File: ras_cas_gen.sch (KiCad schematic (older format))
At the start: 16 parts, among them U10 74HCT02, U11 74LS27, U4 74LS257, U5 74LS257, U6 74LS257, U7 74LS02, U8 74LS138, U9 MOS_6529

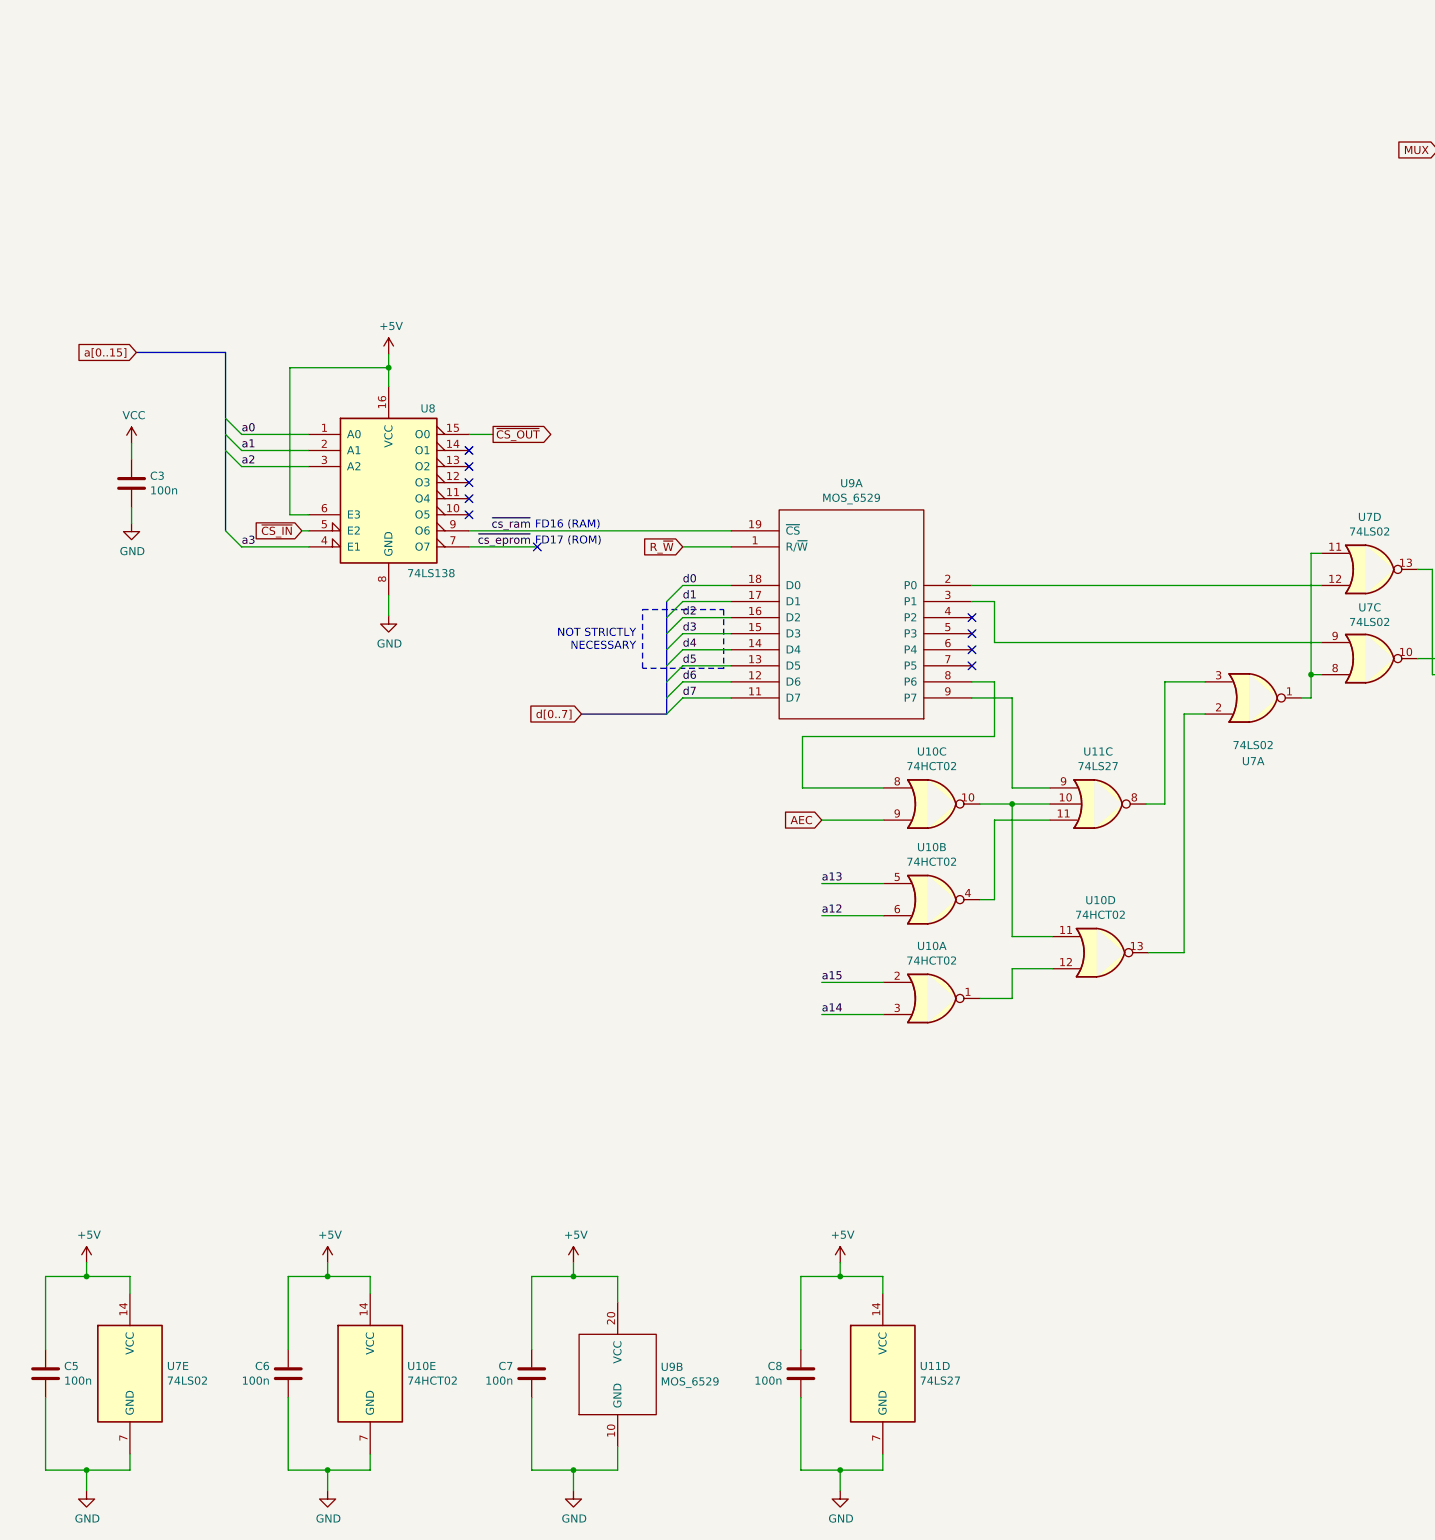
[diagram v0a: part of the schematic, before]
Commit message: Switch out the MOS 6529
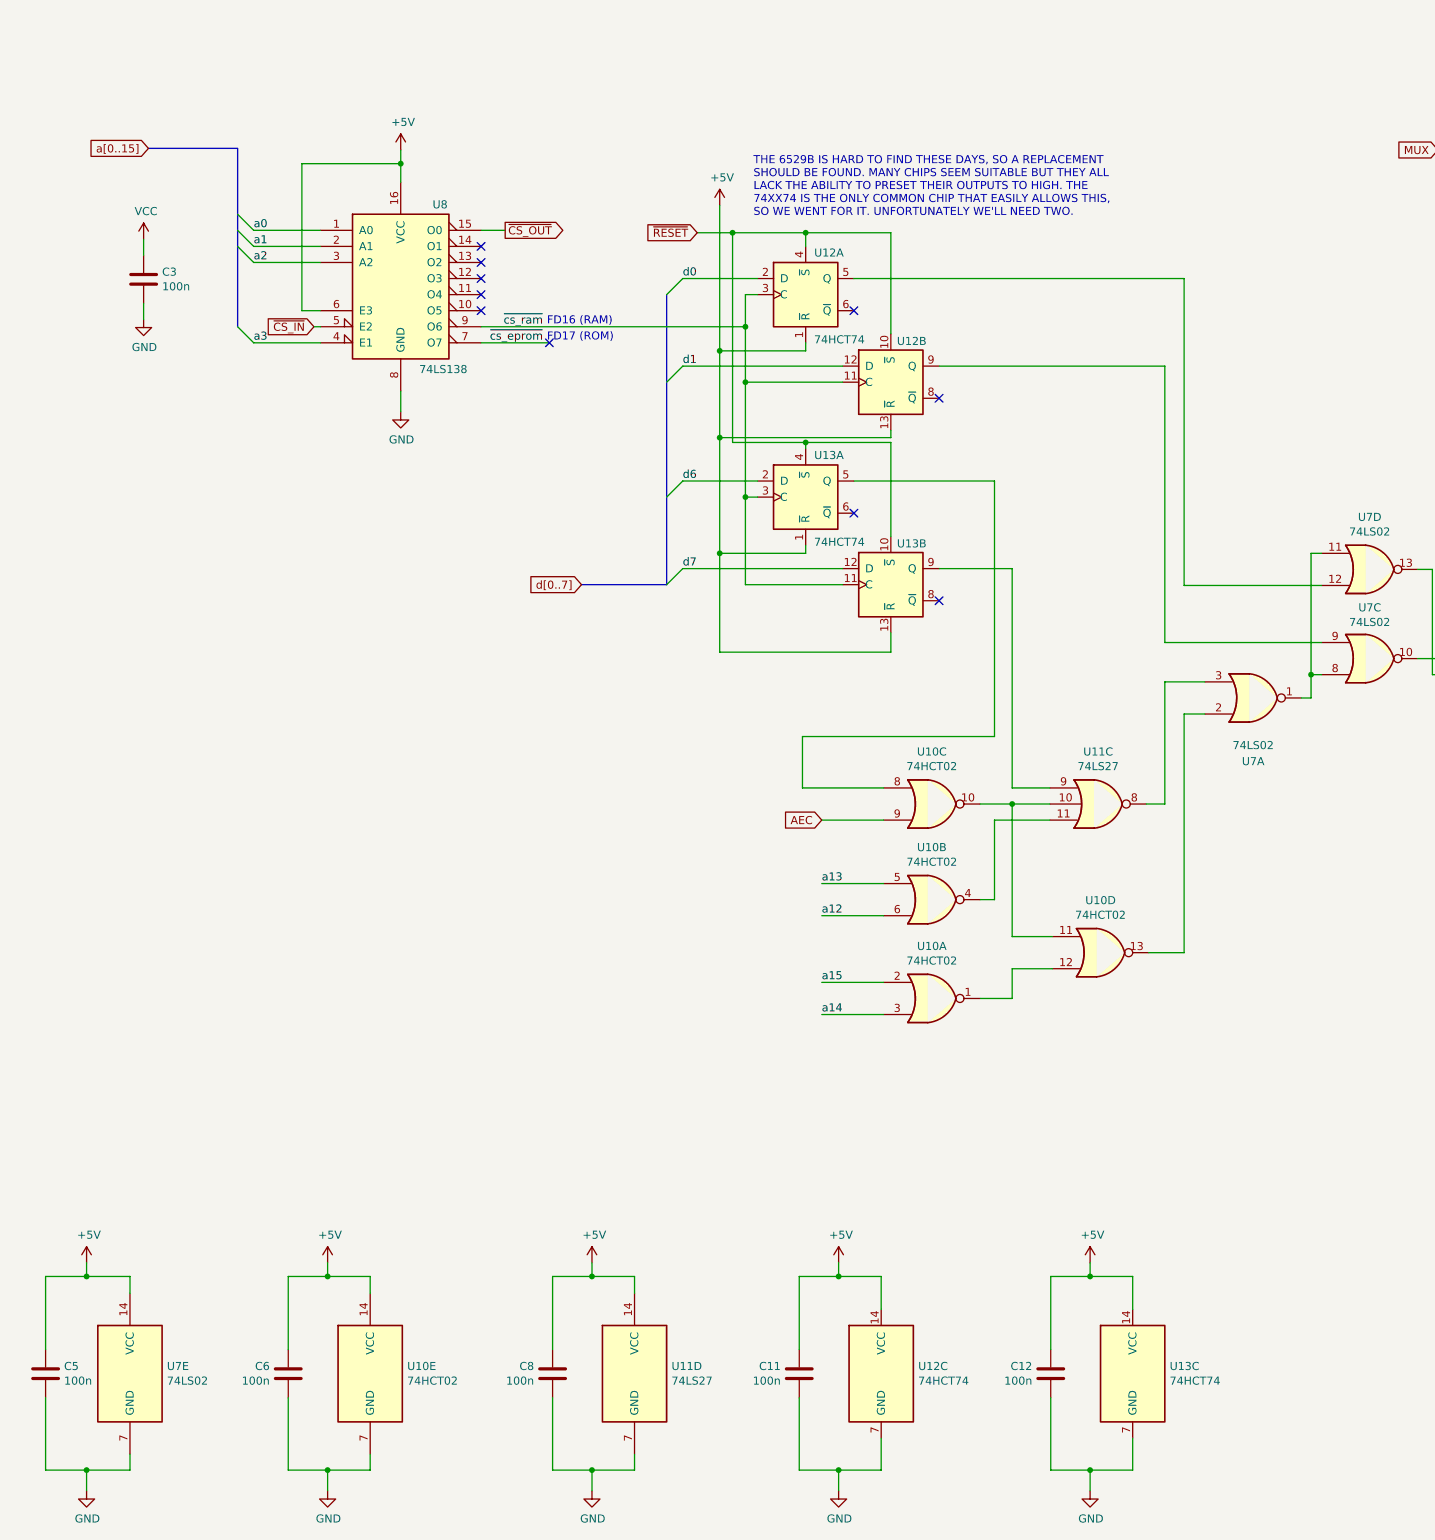
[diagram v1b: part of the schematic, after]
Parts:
- removed C7: 100n, symbol Device:C
- removed U9: MOS_6529, symbol MOS_6529:MOS_6529
- added C11, C12: 100n, symbol Device:C
- added U12, U13: 74HCT74, symbol 74xx:74LS74
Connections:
- net +5V: now also C11.1, C12.1, U12.1 (~R), U12.13 (~R), U12.14 (VCC), U13.1 (~R), U13.13 (~R), U13.14 (VCC)
- net GND: now also C11.2, C12.2, U12.7 (GND), U13.7 (GND)
- net d0: now also U12.2 (D)
- net d1: now also U12.12 (D)
- net d6: now also U13.2 (D)
- net d7: now also U13.12 (D)
- net ~cs_ram: now also U12.11 (C), U12.3 (C), U13.11 (C), U13.3 (C)
- net at U7.12: now also U12.5 (Q)
- net at U7.9: now also U12.9 (Q)
- net at U10.8: now also U13.5 (Q)
- net at U11.9: now also U13.9 (Q)
- new net ~RESET: U12.10 (~S), U12.4 (~S), U13.10 (~S), U13.4 (~S)
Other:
- note added: "THE 6529B IS HARD TO FIND THESE DAYS, SO A REPLACEMENT\nSHOULD BE FOUND. MANY CHIPS SEEM SUITABLE BUT THEY ALL\nLACK THE ABILITY TO PRESET THEIR OUTPUTS TO HIGH. THE\n74XX74 IS THE ONLY COMMON CHIP THAT EASILY ALLOWS THIS,\nSO WE WENT FOR IT. UNFORTUNATELY WE'LL NEED TWO."
- note removed: "NOT STRICTLY\nNECESSARY"
- moved on the sheet: C3, C8, U11D, U8

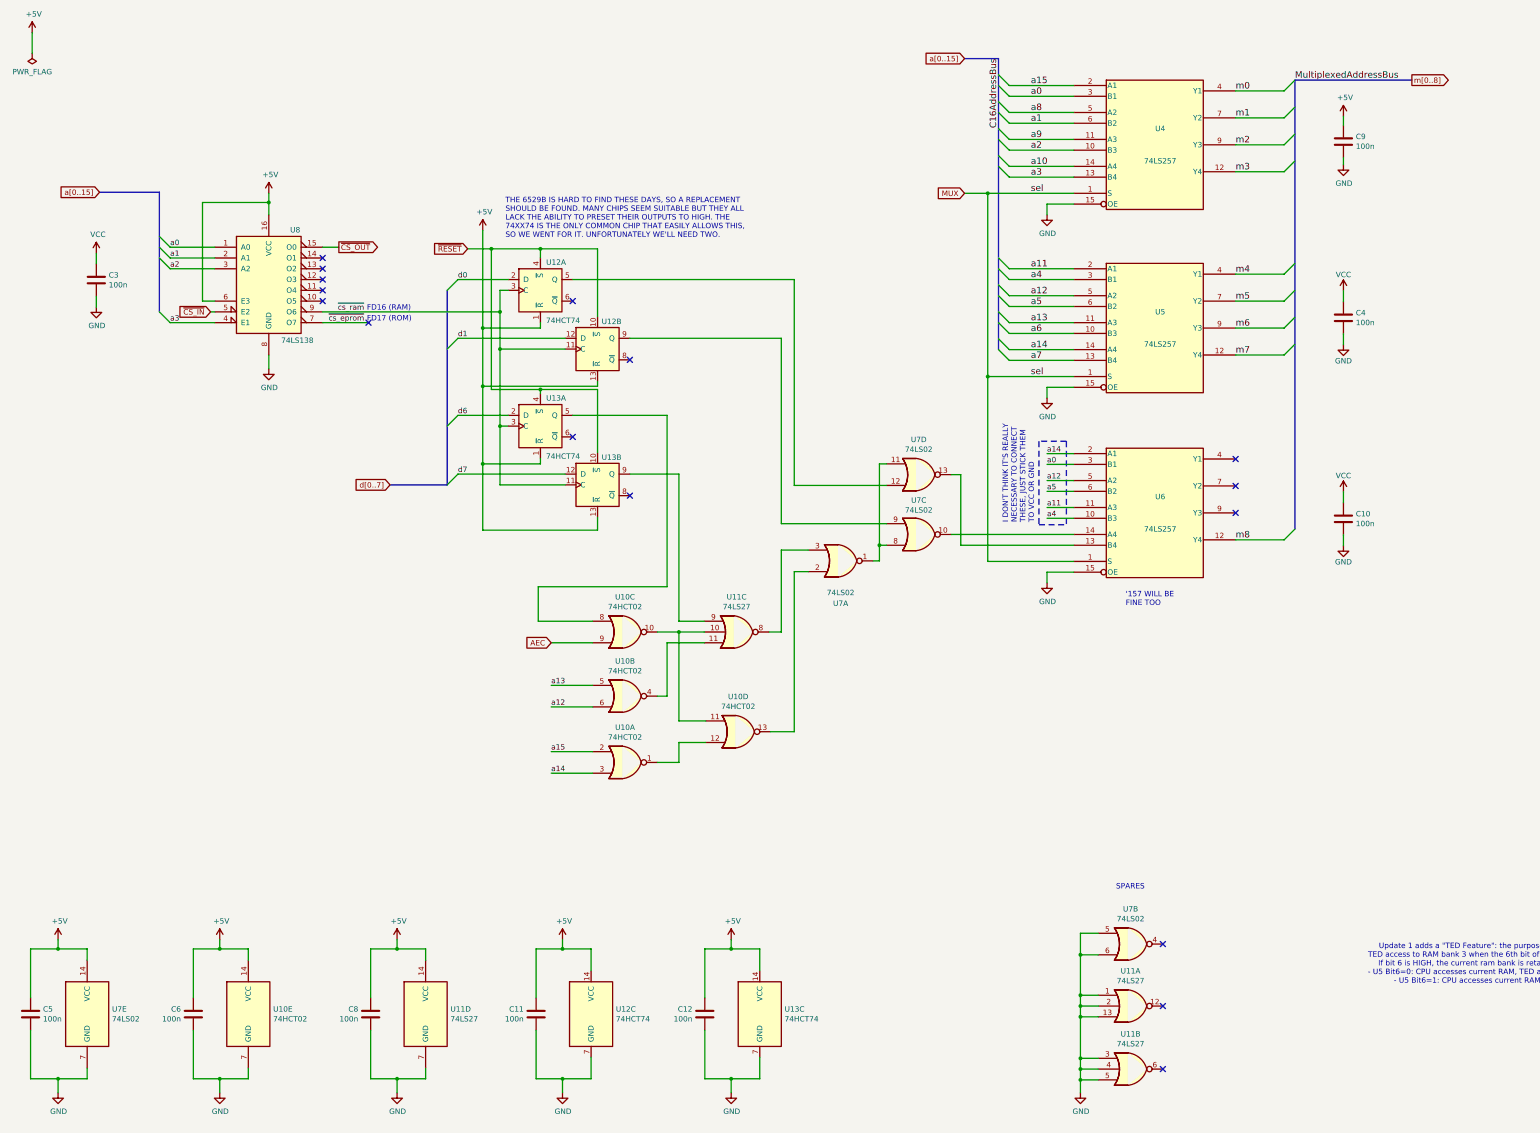
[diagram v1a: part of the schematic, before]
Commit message: Switch all glue logic to a GAL
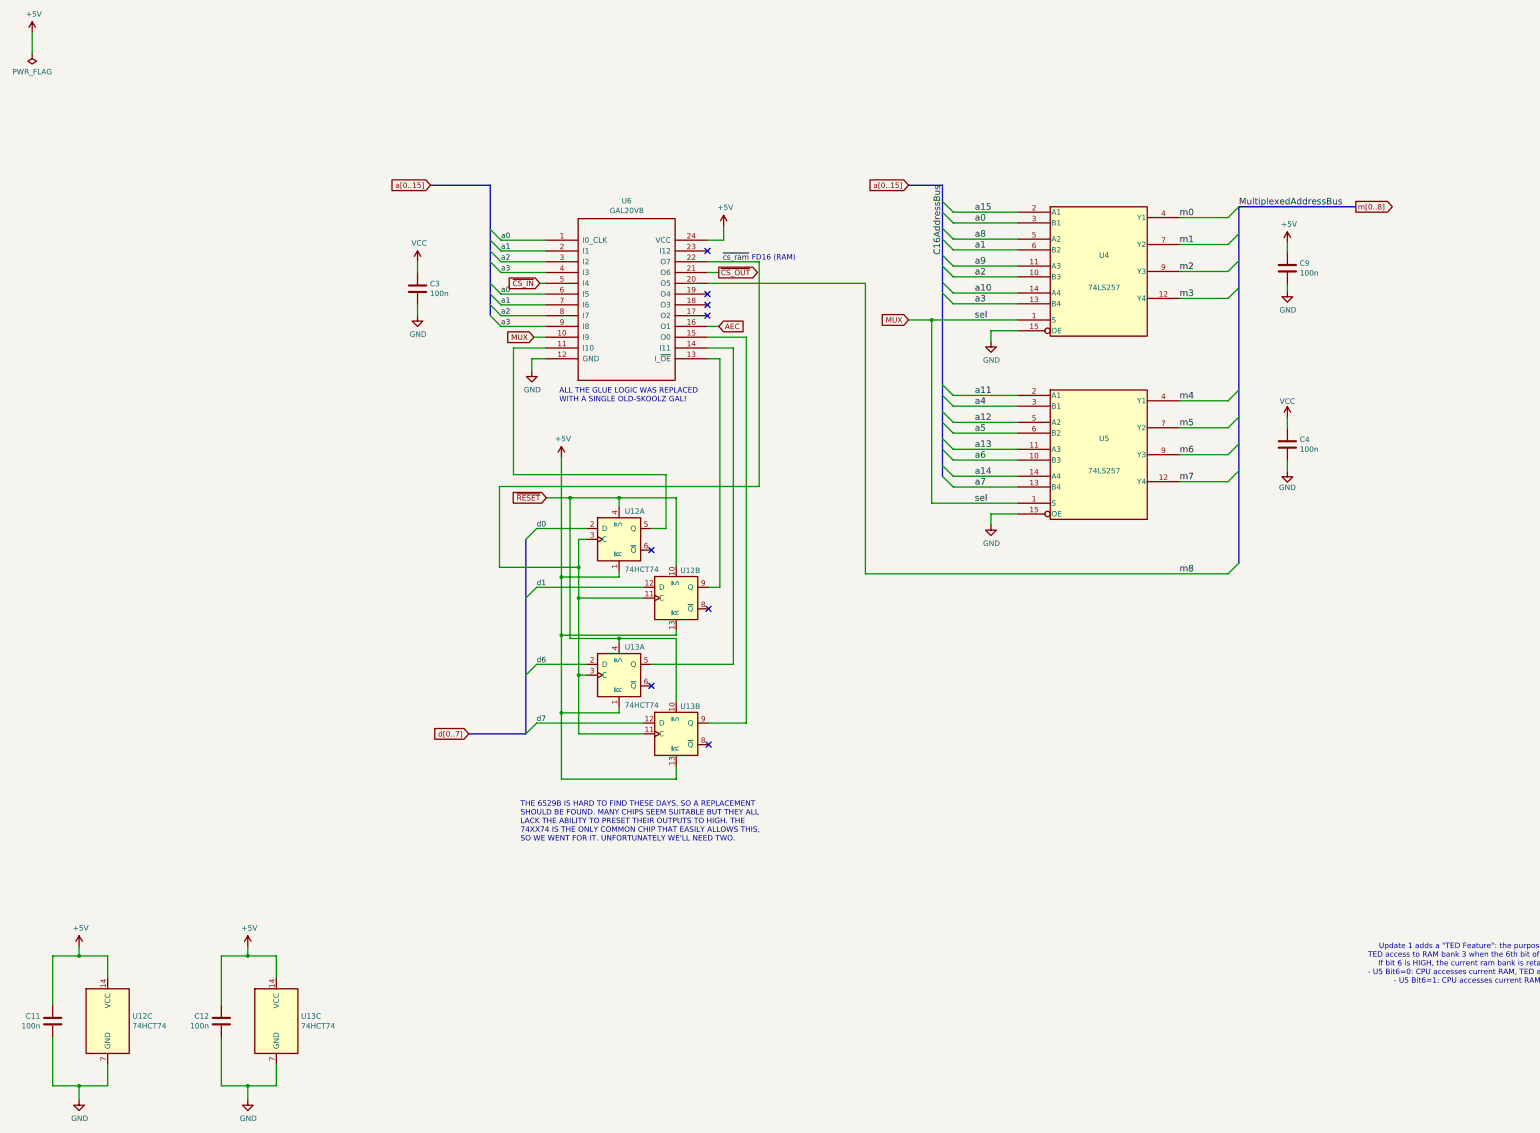
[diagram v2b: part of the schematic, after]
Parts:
- removed C10: 100n, Capacitor_SMD:C_0805_2012Metric_Pad1.18x1.45mm_HandSolder, symbol Device:C
- removed C5, C6, C8: 100n, symbol Device:C
- removed U10: 74HCT02, symbol 74xx:74HCT02
- removed U11: 74LS27, symbol 74xx:74LS27
- removed U6: 74LS257, Package_SO:SOIC-16_3.9x9.9mm_P1.27mm, symbol 74ls257:74LS257
- removed U7: 74LS02, symbol 74xx:74LS02
- removed U8: 74LS138, symbol 74xx:74LS138
- added U6: GAL20V8, MODULE, symbol GAL20V8:GAL20V8
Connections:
- net +5V: now also U6.24 (VCC)
- net AEC: now also U6.16 (O1)
- net GND: now also U6.12 (GND)
- net MUX: now also U6.10 (I9)
- net a0: now also U6.1 (I0_CLK), U6.6 (I5)
- net a1: now also U6.2 (I1), U6.7 (I6)
- net a2: now also U6.3 (I2), U6.8 (I7)
- net a3: now also U6.4 (I3), U6.9 (I8)
- net m8: now also U6.20 (O5)
- net ~CS_IN: now also U6.5 (I4)
- net ~CS_OUT: now also U6.21 (O6)
- net ~cs_ram: now also U6.22 (O7)
- net at U13.5 (Q): now also U6.14 (I11)
- net at U13.9 (Q): now also U6.15 (O0)
- net at U12.9 (Q): now also U6.13 (I_~OE)
- net at U12.5 (Q): now also U6.11 (I10)
- no-connect marks 16 -> 8
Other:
- note added: "ALL THE GLUE LOGIC WAS REPLACED\nWITH A SINGLE OLD-SKOOLZ GAL!"
- note removed: "'157 WILL BE\nFINE TOO"
- note removed: "FD17 (ROM)"
- note removed: "I DON'T THINK IT'S REALLY\nNECESSARY TO CONNECT\nTHESE, JUST STICK THEM\nTO VCC OR GND"
- note removed: "SPARES"
- moved on the sheet: C11, C12, C3, C4, C9, U12A, U12B, U12C, U13A, U13B, U13C, U4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
